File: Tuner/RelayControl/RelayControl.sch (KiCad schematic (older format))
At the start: 69 parts, among them J1 Conn_01x06, J12 Conn_01x01, J13 Conn_01x01, J14 Conn_01x01, J15 Conn_01x01, J2 Conn_02x16_Odd_Even, U1 MCP23017, U2 ULN2803A, U3 ULN2803A

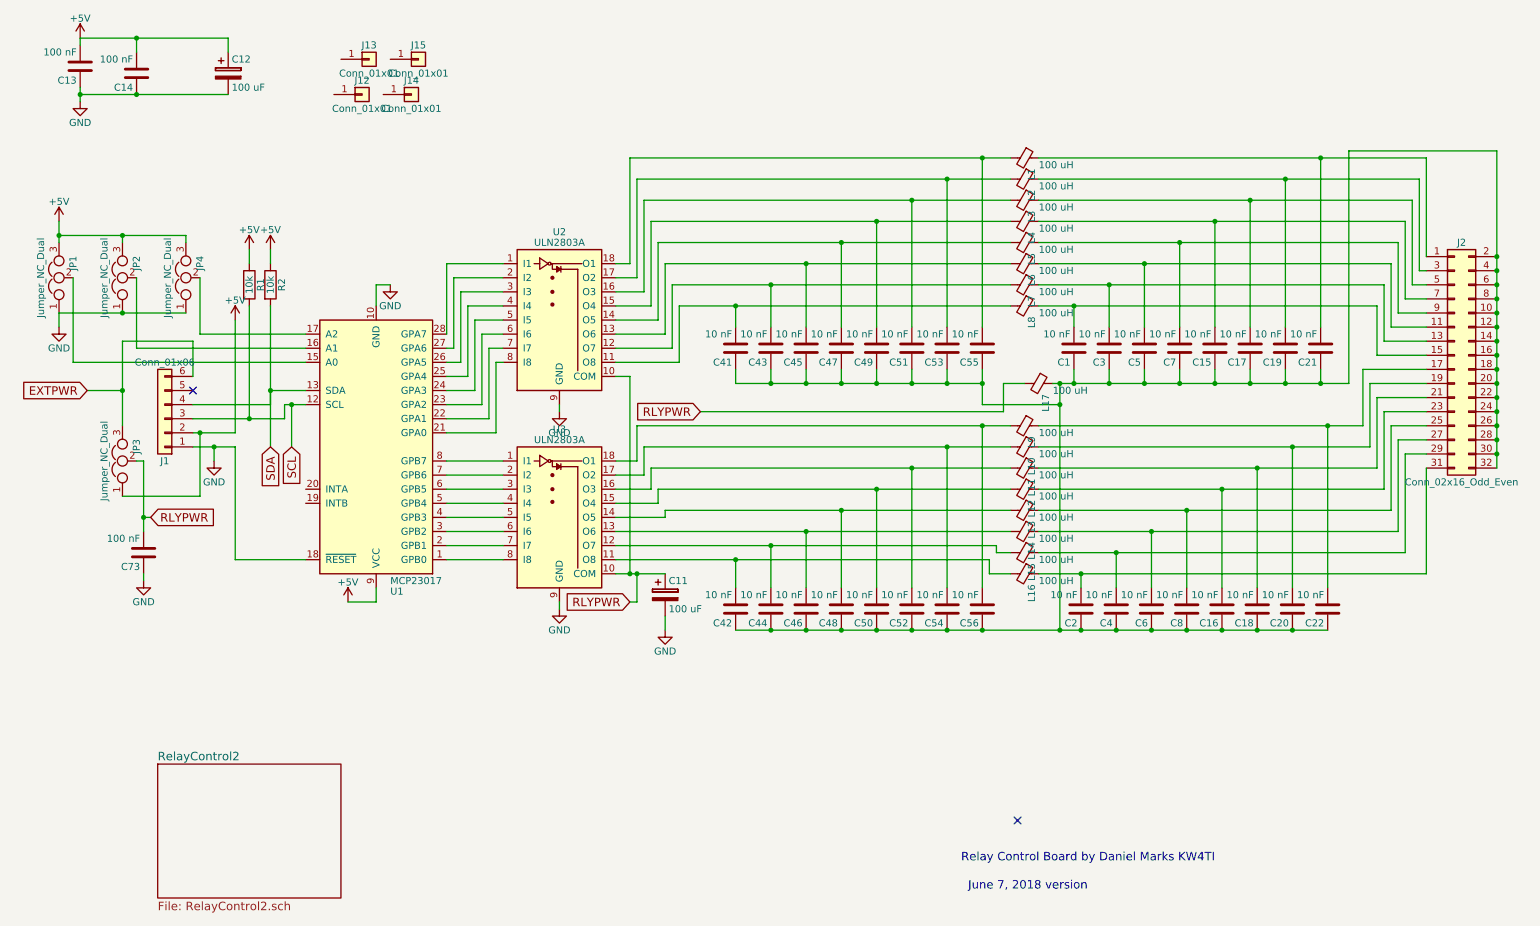
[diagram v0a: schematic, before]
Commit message: Modified RelayControl and Reversible Section to Isolate Digital from Analog sections using RF chokes
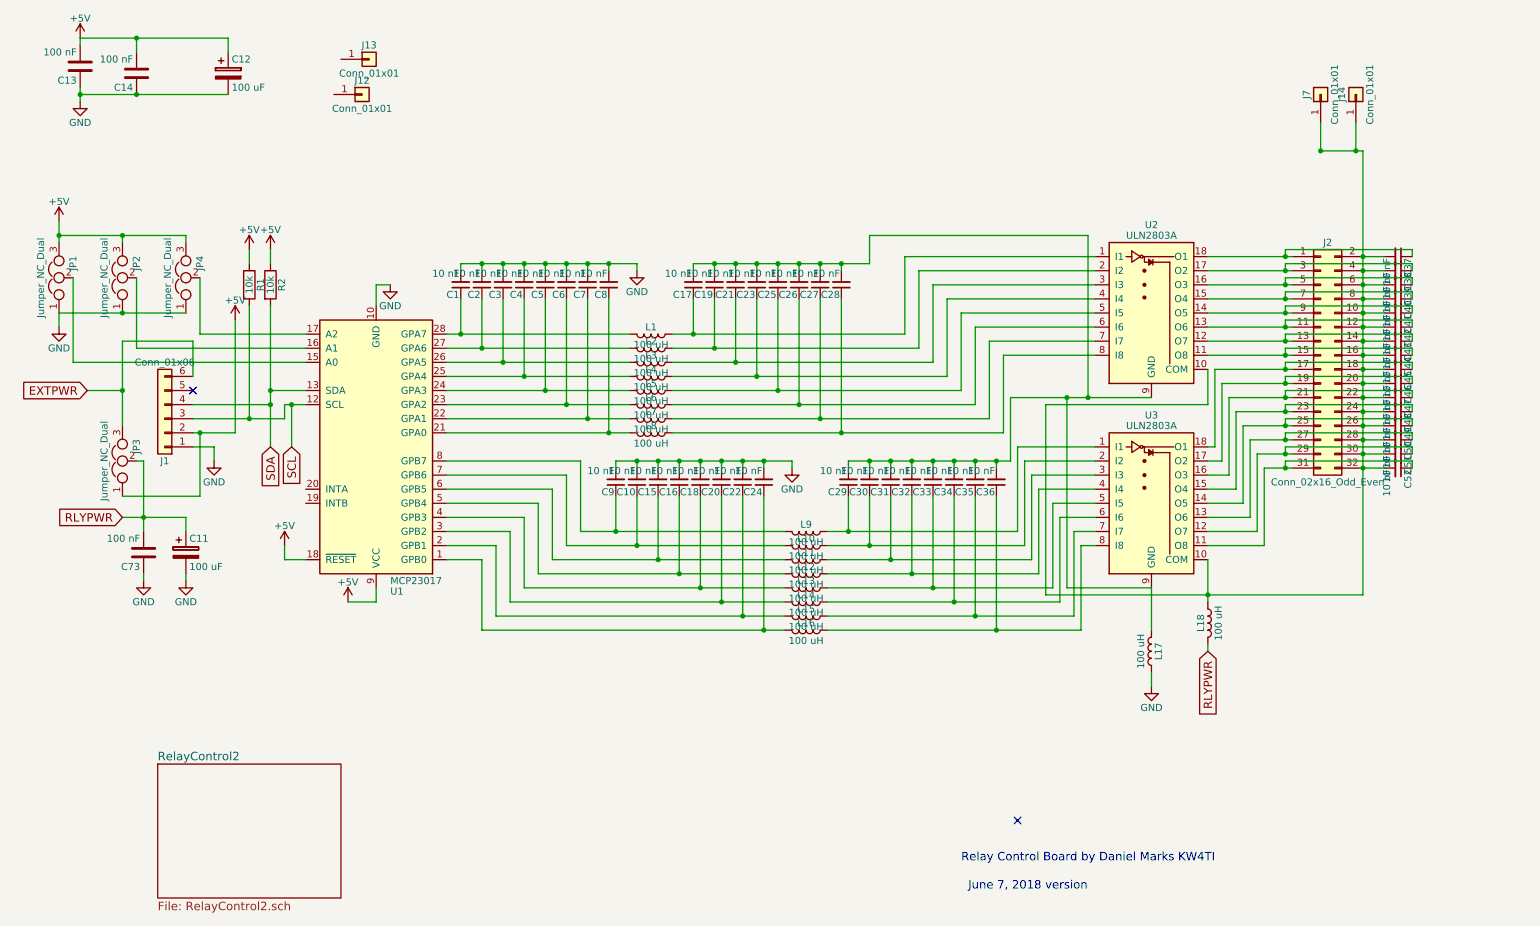
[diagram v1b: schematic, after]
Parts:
- removed C1, C15, C16, C17, C18, C19, C2, C20, C21, C22, C3, C4, C41, C42, C43, C44, C45, C46, C47, C48, C49, C5, C50, C51, C52, C53, C54, C55, C56, C6, C7, C8: 10 nF, Capacitors_THT:C_Disc_D5.0mm_W2.5mm_P2.50mm, symbol C
- removed L1, L10, L11, L12, L13, L14, L15, L16, L17, L2, L3, L4, L5, L6, L7, L8, L9: 100 uH, Inductors_THT:L_Axial_L5.3mm_D2.2mm_P7.62mm_Horizontal_Vishay_IM-1, symbol Ferrite_Bead_Small
- added C1, C10, C15, C16, C17, C18, C19, C2, C20, C21, C22, C23, C24, C25, C26, C27, C28, C29, C3, C30, C31, C32, C33, C34, C35, C36, C37, C38, C39, C4, C40, C41, C42, C43, C44, C45, C46, C47, C48, C49, C5, C50, C51, C52, C6, C7, C8, C9: 10 nF, Capacitors_THT:C_Disc_D5.0mm_W2.5mm_P2.50mm, symbol C_Small
- added L1, L10, L11, L12, L13, L14, L15, L16, L17, L18, L2, L3, L4, L5, L6, L7, L8, L9: 100 uH, Inductors_THT:L_Axial_L5.3mm_D2.2mm_P7.62mm_Horizontal_Vishay_IM-1, symbol L
- renumbered J15 to J7
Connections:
- net +5V: now also U1.18 (~RESET)
- net GND: now also C1.2, C10.2, C15.2, C16.2, C18.2, C2.2, C20.2, C22.2, C24.2, C3.2, C4.2, C5.2, C6.2, C7.2, C8.2, C9.2, L17.1; no longer U1.18 (~RESET), U2.9 (GND), U3.9 (GND)
- net RLYPWR: now also L18.2; no longer U2.10 (COM), U3.10 (COM)
- net at J7.1 (Pin_1): now also J14.1 (Pin_1), J2.10 (Pin_10), J2.12 (Pin_12), J2.14 (Pin_14), J2.16 (Pin_16), J2.18 (Pin_18), J2.2 (Pin_2), J2.20 (Pin_20), J2.22 (Pin_22), J2.24 (Pin_24), J2.26 (Pin_26), J2.28 (Pin_28), J2.30 (Pin_30), J2.32 (Pin_32), J2.4 (Pin_4), J2.6 (Pin_6), J2.8 (Pin_8), U2.10 (COM), U3.10 (COM), C37.2, C38.2, C39.2, C40.2, C41.2, C42.2, C43.2, C44.2, C45.2, C46.2, C47.2, C48.2, C49.2, C50.2, C51.2, C52.2, L18.1
- net at U2.1 (I1): now also C17.1, L1.1; no longer U1.28 (GPA7)
- net at U2.11 (O8): now also J2.15 (Pin_15), C44.1
- net at U2.12 (O7): now also J2.13 (Pin_13), C43.1
- net at U2.13 (O6): now also J2.11 (Pin_11), C42.1
- net at U2.14 (O5): now also J2.9 (Pin_9), C41.1
- net at U2.15 (O4): now also J2.7 (Pin_7), C40.1
- net at U2.16 (O3): now also J2.5 (Pin_5), C39.1
- net at U2.17 (O2): now also J2.3 (Pin_3), C38.1
- net at U2.18 (O1): now also J2.1 (Pin_1), C37.1
- net at U2.2 (I2): now also C19.1, L2.1; no longer U1.27 (GPA6)
- net at U2.3 (I3): now also C21.1, L3.1; no longer U1.26 (GPA5)
- net at U2.4 (I4): now also C23.1, L4.1; no longer U1.25 (GPA4)
- net at U2.5 (I5): now also C25.1, L5.1; no longer U1.24 (GPA3)
- net at U2.6 (I6): now also C26.1, L6.1; no longer U1.23 (GPA2)
- net at U2.7 (I7): now also C27.1, L7.1; no longer U1.22 (GPA1)
- net at U2.8 (I8): now also C28.1, L8.1; no longer U1.21 (GPA0)
- net at U1.1 (GPB0): now also C24.1, L16.2; no longer U3.8 (I8)
- net at U1.2 (GPB1): now also C22.1, L15.2; no longer U3.7 (I7)
- net at U1.3 (GPB2): now also C20.1, L14.2; no longer U3.6 (I6)
- net at U1.4 (GPB3): now also C18.1, L13.2; no longer U3.5 (I5)
- net at U1.5 (GPB4): now also C16.1, L12.2; no longer U3.4 (I4)
- net at U1.6 (GPB5): now also C15.1, L11.2; no longer U3.3 (I3)
- net at U1.7 (GPB6): now also C10.1, L10.2; no longer U3.2 (I2)
- net at U1.8 (GPB7): now also C9.1, L9.2; no longer U3.1 (I1)
- net at U3.11 (O8): now also J2.31 (Pin_31), C52.1
- net at U3.12 (O7): now also J2.29 (Pin_29), C51.1
- net at U3.13 (O6): now also J2.27 (Pin_27), C50.1
- net at U3.14 (O5): now also J2.25 (Pin_25), C49.1
- net at U3.15 (O4): now also J2.23 (Pin_23), C48.1
- net at U3.16 (O3): now also J2.21 (Pin_21), C47.1
- net at U3.17 (O2): now also J2.19 (Pin_19), C46.1
- net at U3.18 (O1): now also J2.17 (Pin_17), C45.1
- new net: C17.2, C19.2, C21.2, C23.2, C25.2, C26.2, C27.2, C28.2, C29.2, C30.2, C31.2, C32.2, C33.2, C34.2, C35.2, C36.2, L17.2, U2.9 (GND), U3.9 (GND)
- new net: C8.1, L8.2, U1.21 (GPA0)
- new net: C7.1, L7.2, U1.22 (GPA1)
- new net: C6.1, L6.2, U1.23 (GPA2)
- new net: C5.1, L5.2, U1.24 (GPA3)
- new net: C4.1, L4.2, U1.25 (GPA4)
- new net: C3.1, L3.2, U1.26 (GPA5)
- new net: C2.1, L2.2, U1.27 (GPA6)
- new net: C1.1, L1.2, U1.28 (GPA7)
- new net: C29.1, L9.1, U3.1 (I1)
- new net: C30.1, L10.1, U3.2 (I2)
- new net: C31.1, L11.1, U3.3 (I3)
- new net: C32.1, L12.1, U3.4 (I4)
- new net: C33.1, L13.1, U3.5 (I5)
- new net: C34.1, L14.1, U3.6 (I6)
- new net: C35.1, L15.1, U3.7 (I7)
- new net: C36.1, L16.1, U3.8 (I8)
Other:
- moved on the sheet: C11, J14, J2, J7, U2, U3

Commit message: Added extra filtering and shunt to RF ground
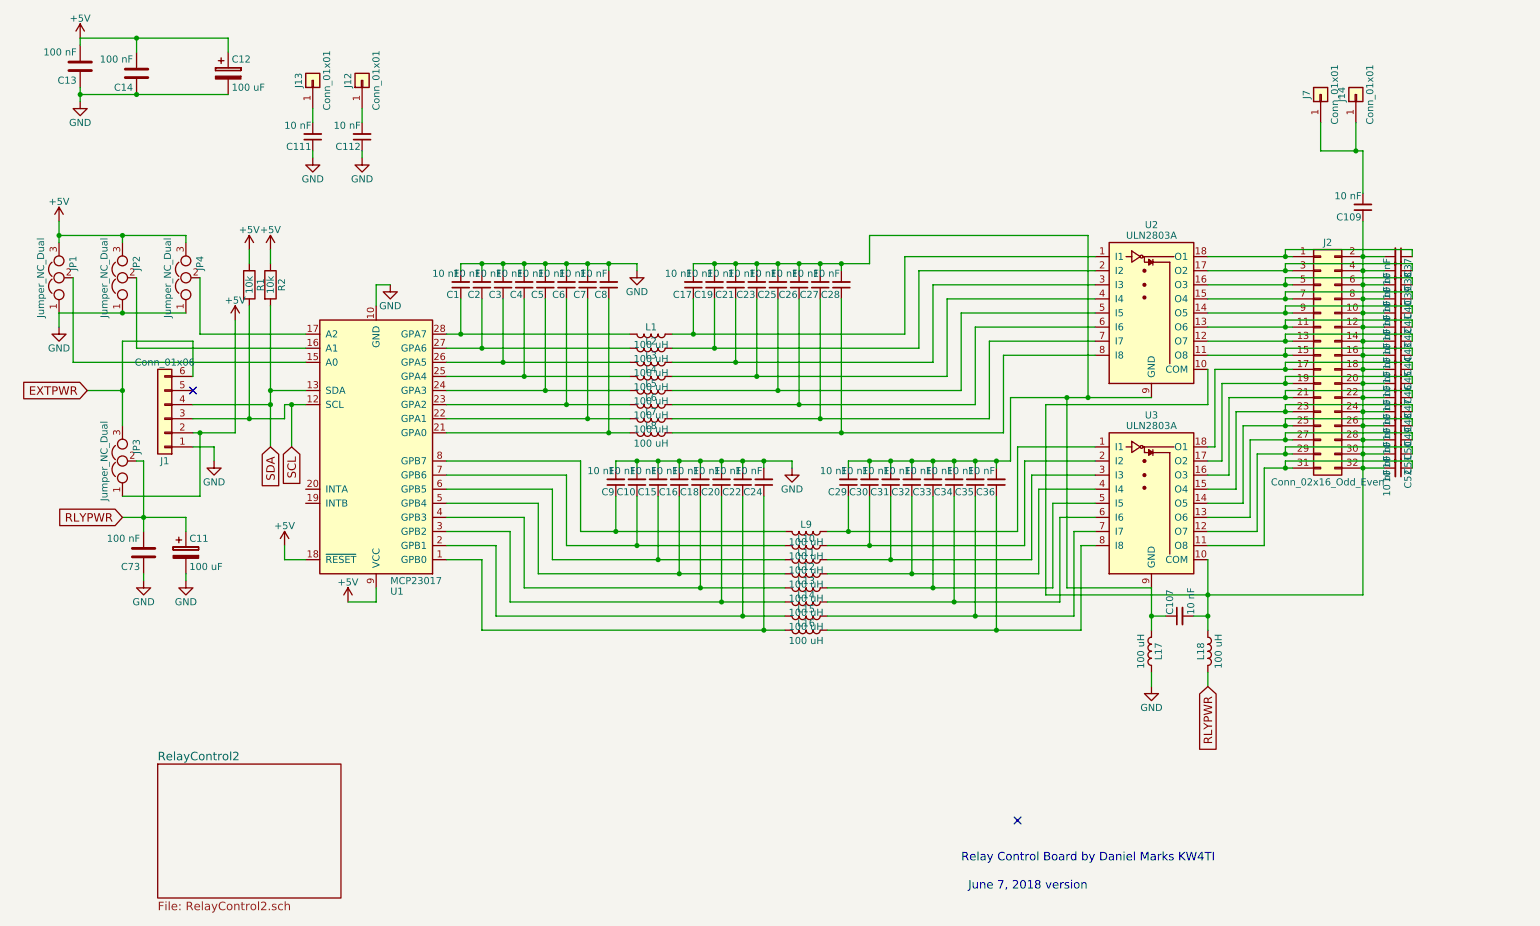
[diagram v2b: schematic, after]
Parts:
- added C107, C109, C111, C112: 10 nF, Capacitors_THT:C_Disc_D5.0mm_W2.5mm_P2.50mm, symbol C_Small
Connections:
- net GND: now also C111.1, C112.1
- net at J13.1 (Pin_1): now also C111.2
- net at C37.2, C38.2, C39.2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: now also C107.2, C109.1; no longer J14.1 (Pin_1), J7.1 (Pin_1)
- net at J12.1 (Pin_1): now also C112.2
- net at C17.2, C19.2, C21.2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: now also C107.1
- new net: C109.2, J14.1 (Pin_1), J7.1 (Pin_1)
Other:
- moved on the sheet: J12, J13, L18
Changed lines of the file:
@@
 L Conn_01x01 J13
 U 1 1 5B19804D
-P 3100 1000
-F 0 "J13" H 3100 1100 50  0000 C CNN
-F 1 "Conn_01x01" H 3100 900 50  0000 C CNN
-F 2 "Connectors:1pin" H 3100 1000 50  0001 C CNN
-F 3 "" H 3100 1000 50  0001 C CNN
-	1    3100 1000
-	1    0    0    -1
+P 2700 1150
+F 0 "J13" H 2700 1250 50  0000 C CNN
+F 1 "Conn_01x01" H 2700 1050 50  0000 C CNN
+F 2 "Connectors:1pin" H 2700 1150 50  0001 C CNN
+F 3 "" H 2700 1150 50  0001 C CNN
+	1    2700 1150
+	0    -1   -1   0
 $EndComp
 $Comp
@@
 L Conn_01x01 J12
 U 1 1 5B1981D8
-P 3050 1250
-F 0 "J12" H 3050 1350 50  0000 C CNN
-F 1 "Conn_01x01" H 3050 1150 50  0000 C CNN
-F 2 "Connectors:1pin" H 3050 1250 50  0001 C CNN
-F 3 "" H 3050 1250 50  0001 C CNN
-	1    3050 1250
-	1    0    0    -1
+P 3050 1150
+F 0 "J12" H 3050 1250 50  0000 C CNN
+F 1 "Conn_01x01" H 3050 1050 50  0000 C CNN
+F 2 "Connectors:1pin" H 3050 1150 50  0001 C CNN
+F 3 "" H 3050 1150 50  0001 C CNN
+	1    3050 1150
+	0    -1   -1   0
 $EndComp
 $Comp
@@
 $EndComp
 $Comp
-L GND #PWR13
+L GND #PWR15
 U 1 1 5B8A94DA
 P 3250 2600
-F 0 "#PWR13" H 3250 2350 50  0001 C CNN
+F 0 "#PWR15" H 3250 2350 50  0001 C CNN
 F 1 "GND" H 3250 2450 50  0000 C CNN
 F 2 "" H 3250 2600 50  0001 C CNN
@@
 RLYPWR
 $Comp
-L +5V #PWR12
+L +5V #PWR13
 U 1 1 5B8AAB56
 P 2950 4850
-F 0 "#PWR12" H 2950 4700 50  0001 C CNN
+F 0 "#PWR13" H 2950 4700 50  0001 C CNN
 F 1 "+5V" H 2950 4990 50  0000 C CNN
 F 2 "" H 2950 4850 50  0001 C CNN
@@
 $EndComp
 $Comp
-L GND #PWR16
+L GND #PWR18
 U 1 1 5B97EDC9
 P 8650 5450
-F 0 "#PWR16" H 8650 5200 50  0001 C CNN
+F 0 "#PWR18" H 8650 5200 50  0001 C CNN
 F 1 "GND" H 8650 5300 50  0000 C CNN
 F 2 "" H 8650 5450 50  0001 C CNN
@@
 L L L18
 U 1 1 5B98C045
-P 9050 5000
-F 0 "L18" V 9000 5000 50  0000 C CNN
-F 1 "100 uH" V 9125 5000 50  0000 C CNN
-F 2 "Inductors_THT:L_Axial_L5.3mm_D2.2mm_P7.62mm_Horizontal_Vishay_IM-1" H 9050 5000 50  0001 C CNN
-F 3 "" H 9050 5000 50  0001 C CNN
-	1    9050 5000
-	1    0    0    -1
-$EndComp
-Text GLabel 9050 5200 3    60   Input ~ 0
+P 9050 5200
+F 0 "L18" V 9000 5200 50  0000 C CNN
+F 1 "100 uH" V 9125 5200 50  0000 C CNN
+F 2 "Inductors_THT:L_Axial_L5.3mm_D2.2mm_P7.62mm_Horizontal_Vishay_IM-1" H 9050 5200 50  0001 C CNN
+F 3 "" H 9050 5200 50  0001 C CNN
+	1    9050 5200
+	1    0    0    -1
+$EndComp
+Text GLabel 9050 5450 3    60   Input ~ 0
 RLYPWR
 $Comp
@@
 $EndComp
 $Comp
-L GND #PWR14
+L GND #PWR16
 U 1 1 5B992951
 P 5000 2500
-F 0 "#PWR14" H 5000 2250 50  0001 C CNN
+F 0 "#PWR16" H 5000 2250 50  0001 C CNN
 F 1 "GND" H 5000 2350 50  0000 C CNN
 F 2 "" H 5000 2500 50  0001 C CNN
@@
 $EndComp
 $Comp
-L GND #PWR15
+L GND #PWR17
 U 1 1 5B998DAB
 P 6100 3900
-F 0 "#PWR15" H 6100 3650 50  0001 C CNN
+F 0 "#PWR17" H 6100 3650 50  0001 C CNN
 F 1 "GND" H 6100 3750 50  0000 C CNN
 F 2 "" H 6100 3900 50  0001 C CNN
@@
 	-1   0    0    1
 $EndComp
+$Comp
+L C_Small C107
+U 1 1 5B9702E0
+P 8850 4950
+F 0 "C107" H 8860 5020 50  0000 L CNN
+F 1 "10 nF" H 8860 4870 50  0000 L CNN
+F 2 "Capacitors_THT:C_Disc_D5.0mm_W2.5mm_P2.50mm" H 8850 4950 50  0001 C CNN
+F 3 "" H 8850 4950 50  0001 C CNN
+	1    8850 4950
+	0    -1   -1   0
+$EndComp
+$Comp
+L C_Small C109
+U 1 1 5B97B2C6
+P 10150 2050
+F 0 "C109" H 10160 2120 50  0000 L CNN
+F 1 "10 nF" H 10160 1970 50  0000 L CNN
+F 2 "Capacitors_THT:C_Disc_D5.0mm_W2.5mm_P2.50mm" H 10150 2050 50  0001 C CNN
+F 3 "" H 10150 2050 50  0001 C CNN
+	1    10150 2050
+	-1   0    0    1
+$EndComp
+$Comp
+L C_Small C111
+U 1 1 5B97FFF6
+P 2700 1550
+F 0 "C111" H 2710 1620 50  0000 L CNN
+F 1 "10 nF" H 2710 1470 50  0000 L CNN
+F 2 "Capacitors_THT:C_Disc_D5.0mm_W2.5mm_P2.50mm" H 2700 1550 50  0001 C CNN
+F 3 "" H 2700 1550 50  0001 C CNN
+	1    2700 1550
+	-1   0    0    1
+$EndComp
+$Comp
+L C_Small C112
+U 1 1 5B980336
+P 3050 1550
+F 0 "C112" H 3060 1620 50  0000 L CNN
+F 1 "10 nF" H 3060 1470 50  0000 L CNN
+F 2 "Capacitors_THT:C_Disc_D5.0mm_W2.5mm_P2.50mm" H 3050 1550 50  0001 C CNN
+F 3 "" H 3050 1550 50  0001 C CNN
+	1    3050 1550
+	-1   0    0    1
+$EndComp
+$Comp
+L GND #PWR12
+U 1 1 5B980926
+P 2700 1700
+F 0 "#PWR12" H 2700 1450 50  0001 C CNN
+F 1 "GND" H 2700 1550 50  0000 C CNN
+F 2 "" H 2700 1700 50  0001 C CNN
+F 3 "" H 2700 1700 50  0001 C CNN
+	1    2700 1700
+	1    0    0    -1
+$EndComp
+$Comp
+L GND #PWR14
+U 1 1 5B980A3F
+P 3050 1700
+F 0 "#PWR14" H 3050 1450 50  0001 C CNN
+F 1 "GND" H 3050 1550 50  0000 C CNN
+F 2 "" H 3050 1700 50  0001 C CNN
+F 3 "" H 3050 1700 50  0001 C CNN
+	1    3050 1700
+	1    0    0    -1
+$EndComp
 Connection ~ 4800 2450
 Wire Wire Line
@@
 Connection ~ 10150 3900
 Wire Wire Line
-	9050 4550 9050 4850
+	9050 4550 9050 5050
 Wire Wire Line
 	10150 4800 7900 4800
@@
 Wire Wire Line
 	9050 2400 9650 2400
-Connection ~ 9850 1650
 Wire Wire Line
 	9850 1650 9850 1450
-Connection ~ 10100 1650
 Wire Wire Line
 	10100 1450 10100 1650
@@
 Connection ~ 10150 2500
 Wire Wire Line
-	10150 1650 10150 4800
-Wire Wire Line
 	3150 4850 3150 4750
 Wire Wire Line
@@
 	8650 5450 8650 5350
 Wire Wire Line
-	9050 5150 9050 5200
+	9050 5350 9050 5450
 Wire Wire Line
 	7950 4750 7950 4150
@@
 	2400 2750 2400 3750
 Connection ~ 2400 3450
+Wire Wire Line
+	8750 4950 8650 4950
+Connection ~ 8650 4950
+Wire Wire Line
+	8950 4950 9050 4950
+Connection ~ 9050 4950
+Wire Wire Line
+	10150 2150 10150 4800
+Wire Wire Line
+	10150 1650 10150 1950
+Connection ~ 10100 1650
+Wire Wire Line
+	3050 1350 3050 1450
+Wire Wire Line
+	2700 1350 2700 1450
+Wire Wire Line
+	3050 1650 3050 1700
+Wire Wire Line
+	2700 1650 2700 1700
 $EndSCHEMATC
